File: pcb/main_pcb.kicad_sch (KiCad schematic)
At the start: 39 parts, among them J1 Conn_01x06_Socket, J2 Conn_01x10_Pin, J3 Conn_01x06_Pin, J4 USB_C_Receptacle_USB2.0, Q1 Si2323DS, SW1 SW_Push, SW2 SW_Push, SW3 SW_Push, U1 ESP32-H2-MINI-1, U2 LM5165Y

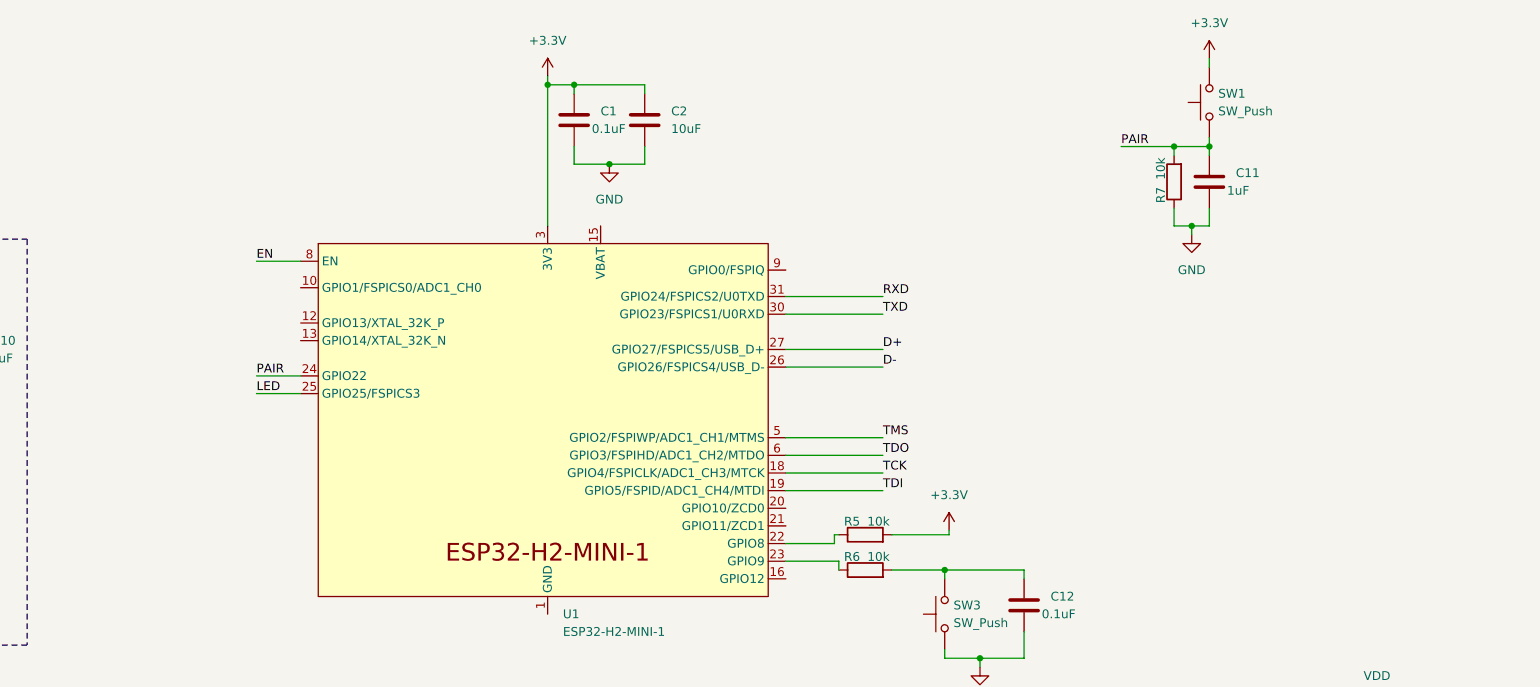
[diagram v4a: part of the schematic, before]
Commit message: Add RTC crystal circuit
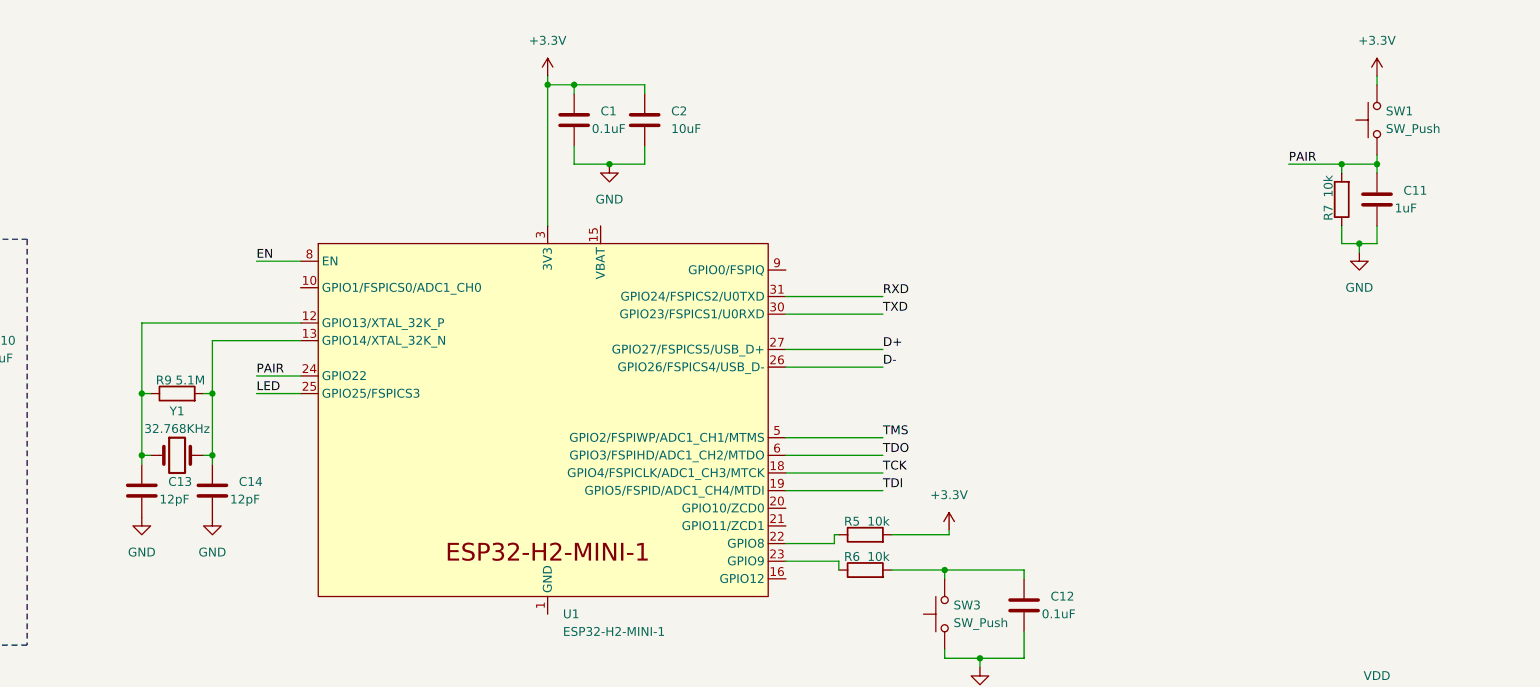
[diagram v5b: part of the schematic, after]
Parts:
- added C13, C14: 12pF, Capacitor_SMD:C_1206_3216Metric_Pad1.33x1.80mm_HandSolder, symbol Device:C
- added R9: 5.1M, Resistor_SMD:R_1206_3216Metric_Pad1.30x1.75mm_HandSolder, symbol Device:R
- added Y1: 32.768KHz, Crystal:Crystal_SMD_Abracon_ABS25-4Pin_8.0x3.8mm, symbol Device:Crystal
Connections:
- net GND: now also C13.2, C14.2
- net at U1.12 (GPIO13/XTAL_32K_P): now also C13.1, R9.1, Y1.1
- net at U1.13 (GPIO14/XTAL_32K_N): now also C14.1, R9.2, Y1.2
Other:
- moved on the sheet: C11, R7, SW1

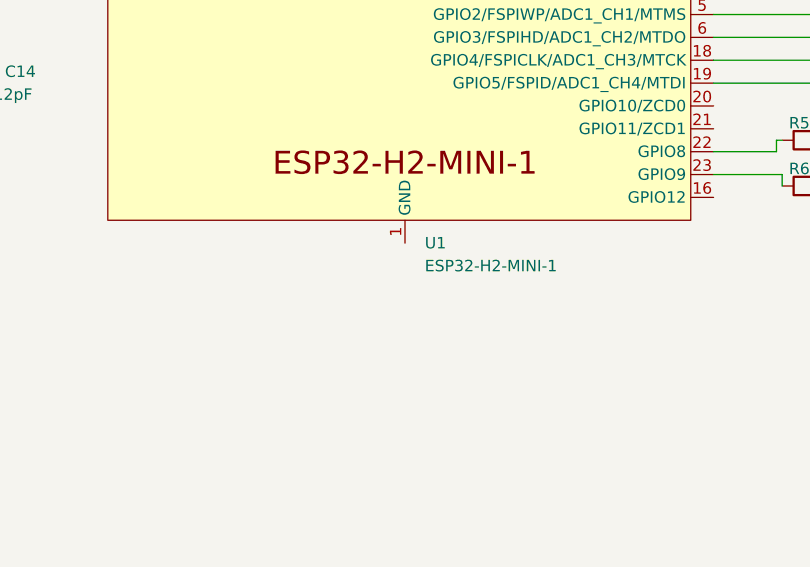
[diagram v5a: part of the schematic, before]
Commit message: Add GND connection to ESP32-H2
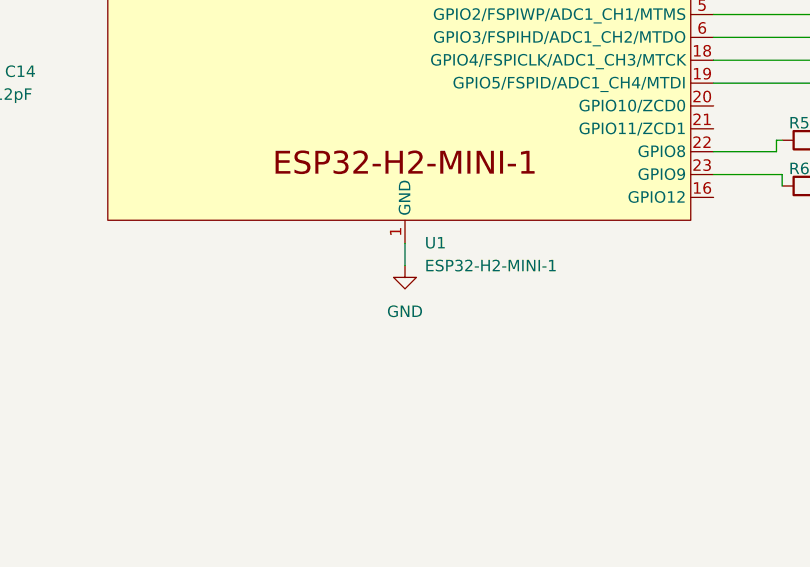
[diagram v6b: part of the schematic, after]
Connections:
- net GND: now also U1.1 (GND), U1.11 (GND), U1.14 (GND), U1.2 (GND), U1.36 (GND), U1.37 (GND), U1.38 (GND), U1.39 (GND), U1.40 (GND), U1.41 (GND), U1.42 (GND), U1.43 (GND), U1.44 (GND), U1.45 (GND), U1.46 (GND), U1.47 (GND), U1.48 (GND), U1.49 (GND), U1.50 (GND), U1.51 (GND), U1.52 (GND), U1.53 (GND)
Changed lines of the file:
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@@
+    (stroke (width 0) (type default))
+  )
+  (wire (pts (xy 158.75 105.41) (xy 158.75 107.95))
     (stroke (width 0) (type default))
   )
@@
         )
       )
+    )
+  )
+  (symbol (lib_id "power:GND") (at 158.75 107.95 0) (unit 1)
+    (in_bom yes) (on_board yes) (dnp no) (fields_autoplaced)
+    (property "Reference" "#PWR037" (at 158.75 114.3 0)
+      (effects (font (size 1.27 1.27)) hide)
+    )
+    (property "Value" "GND" (at 158.75 113.03 0)
+      (effects (font (size 1.27 1.27)))
+    )
+    (property "Footprint" "" (at 158.75 107.95 0)
+      (effects (font (size 1.27 1.27)) hide)
+    )
+    (property "Datasheet" "" (at 158.75 107.95 0)
+      (effects (font (size 1.27 1.27)) hide)
+    )
+    (pin "1")
+    (instances
+      (project "main_pcb"
+        (path "/6204b7c2-8814-41ee-9243-5078f55f08d4"
+          (reference "#PWR037") (unit 1)
+        )
+      )

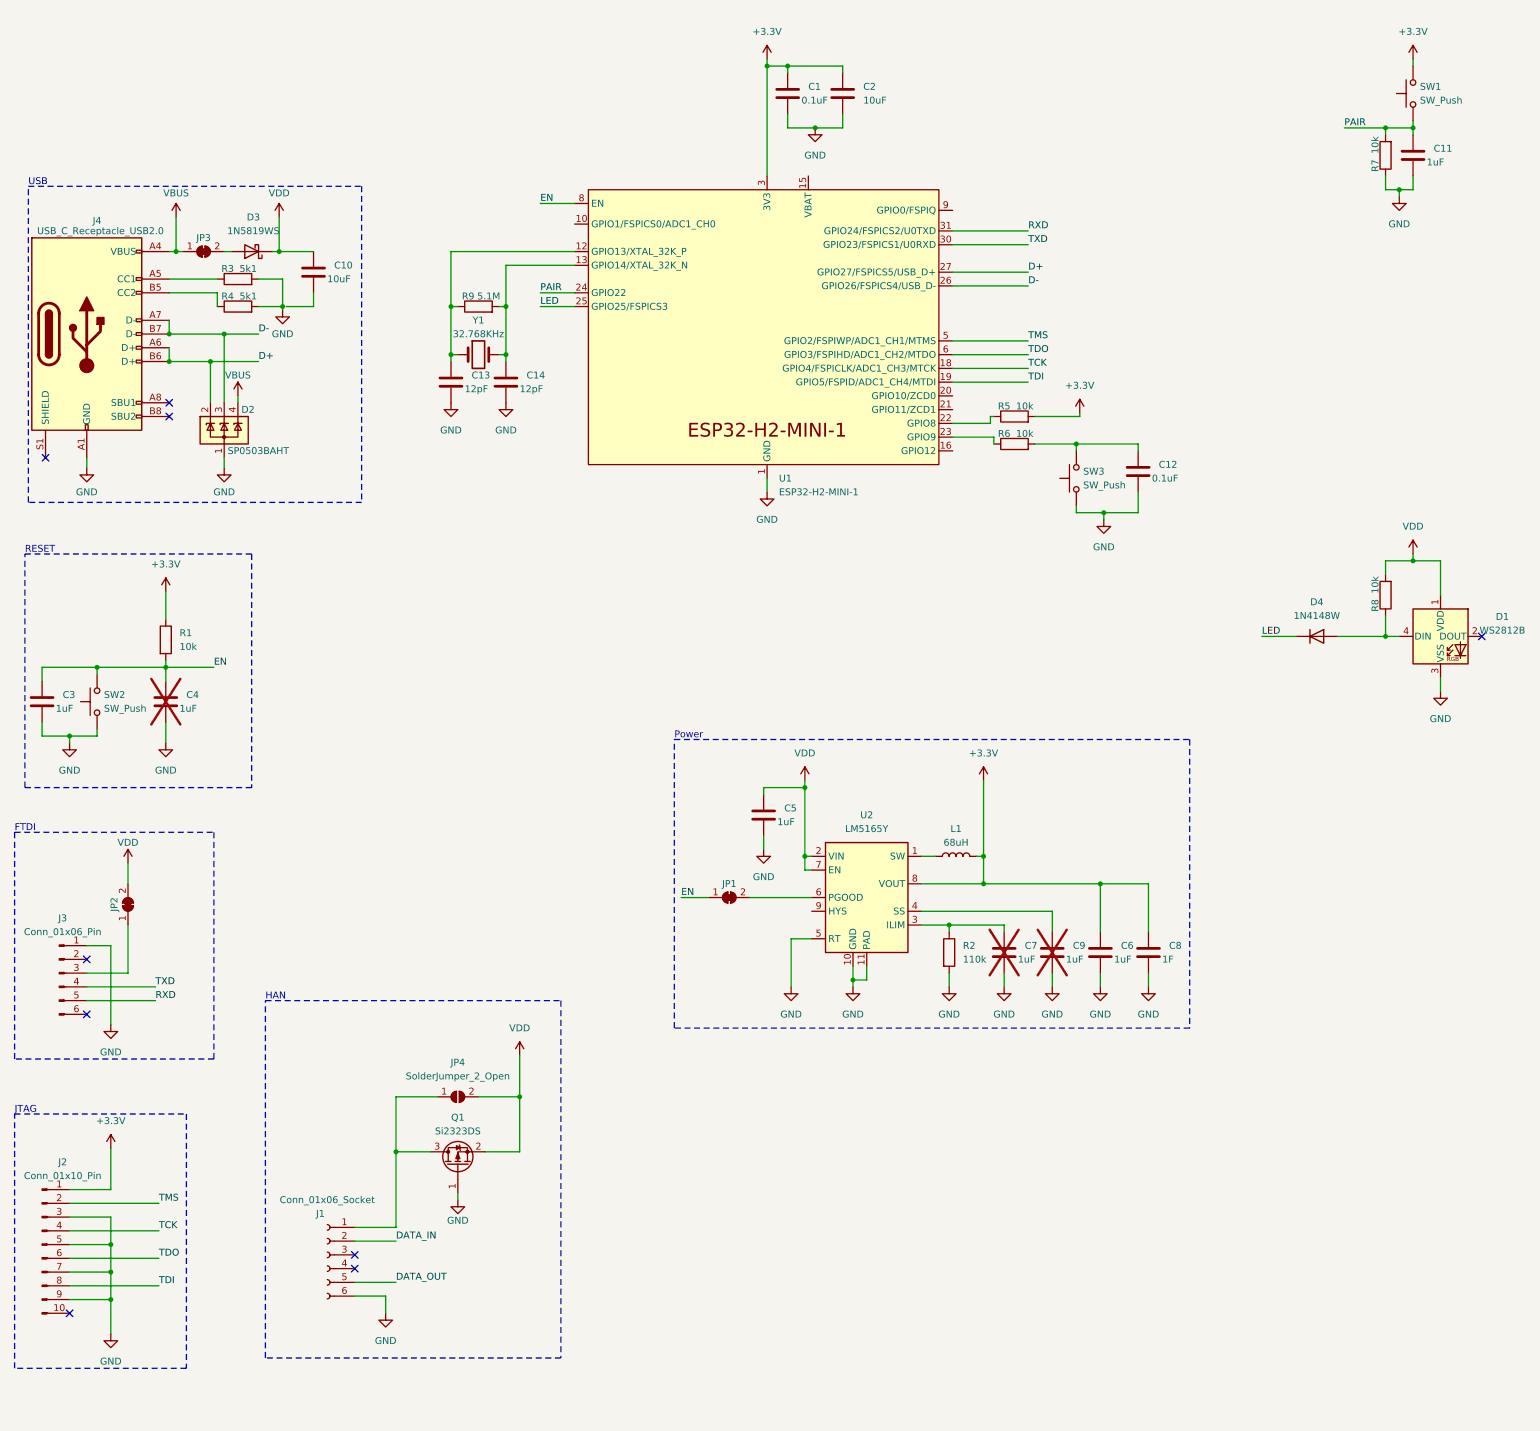
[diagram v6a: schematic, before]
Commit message: Remove FTDI connector
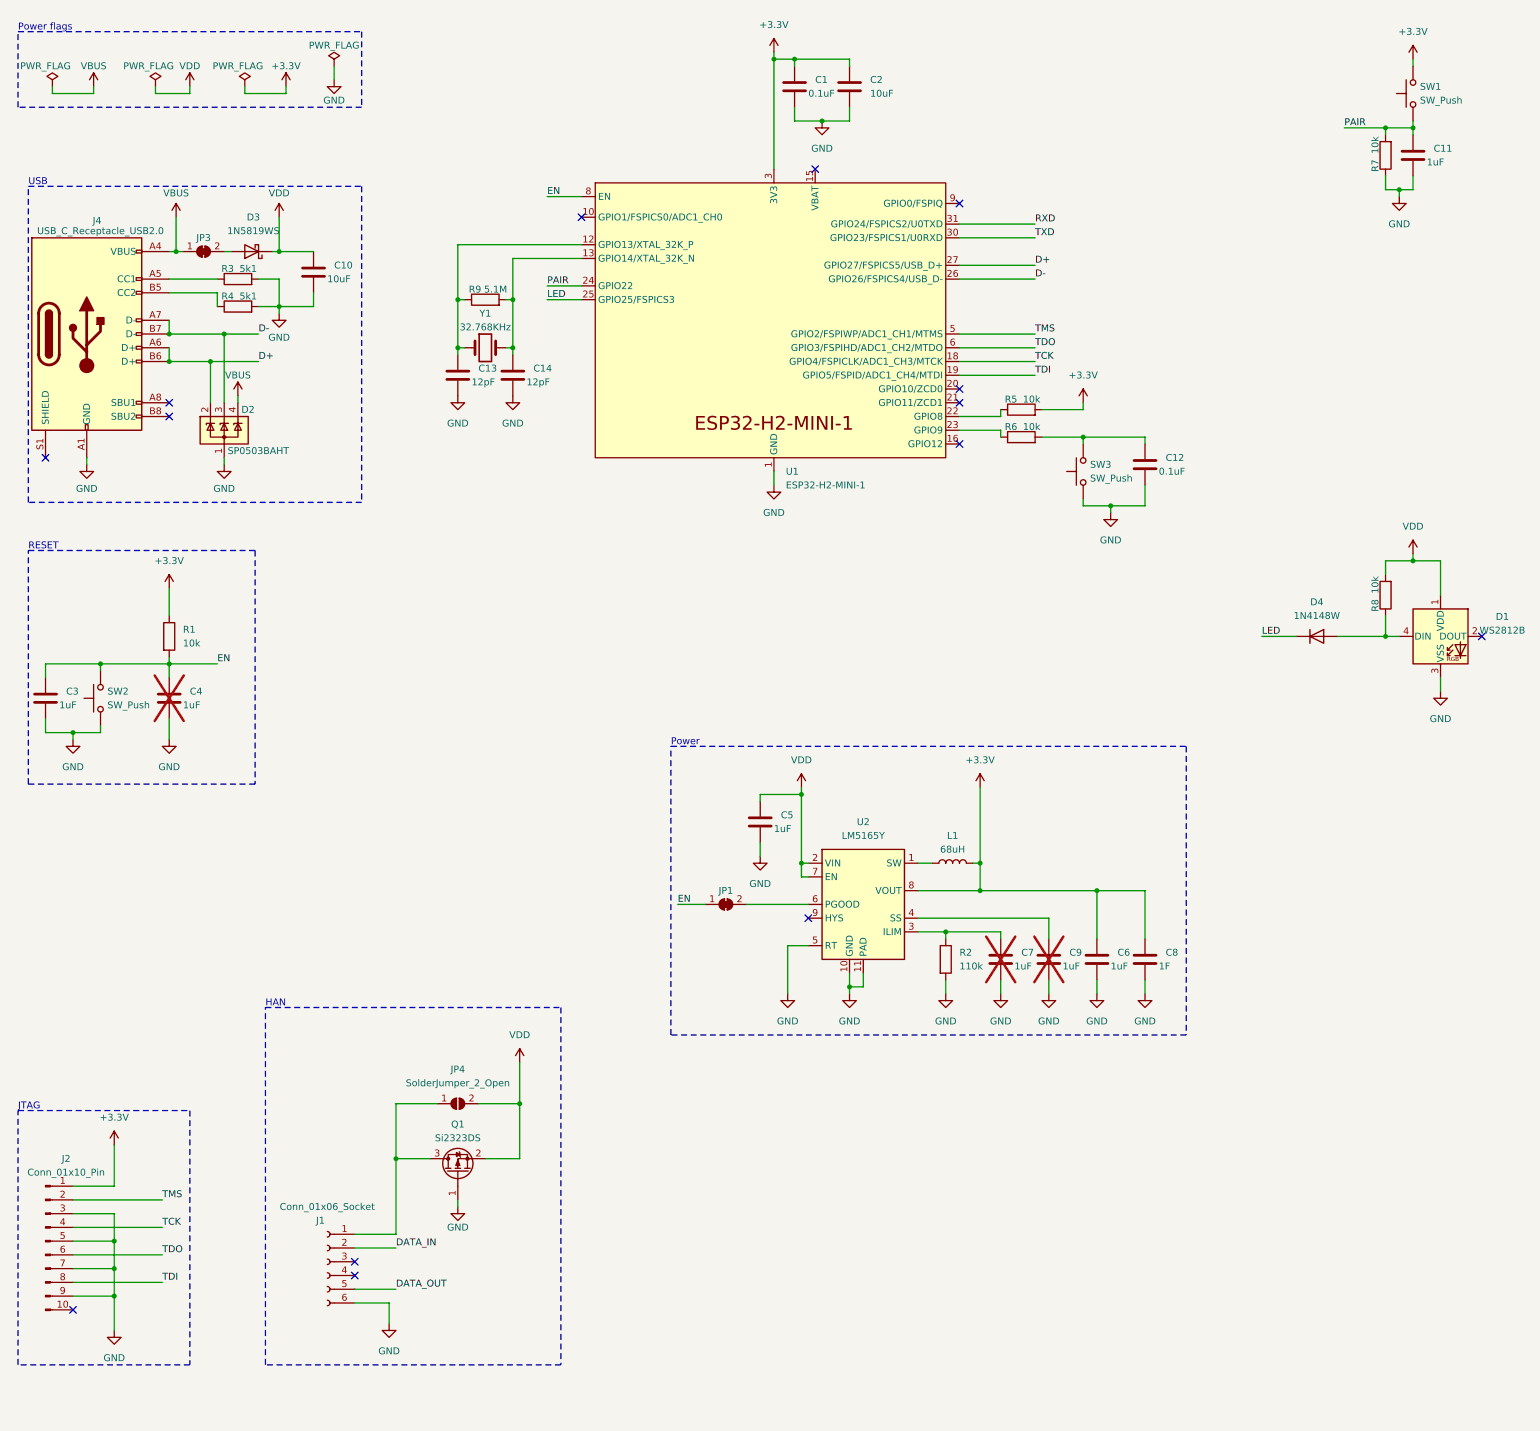
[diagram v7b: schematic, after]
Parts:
- removed J3: Conn_01x06_Pin, Connector_PinHeader_2.54mm:PinHeader_1x06_P2.54mm_Horizontal, symbol Connector:Conn_01x06_Pin
- removed JP2: SolderJumper_2_Bridged, Jumper:SolderJumper-2_P1.3mm_Open_TrianglePad1.0x1.5mm, symbol Jumper:SolderJumper_2_Bridged
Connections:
- net GND: now also C10.2
- no-connect marks 9 -> 14
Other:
- note added: "Power flags"
- note removed: "FTDI"
- moved on the sheet: C1, C12, C13, C14, C2, C3, C4, C5, C6, C7, C8, C9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

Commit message: Add HAN interface connections to ESP32
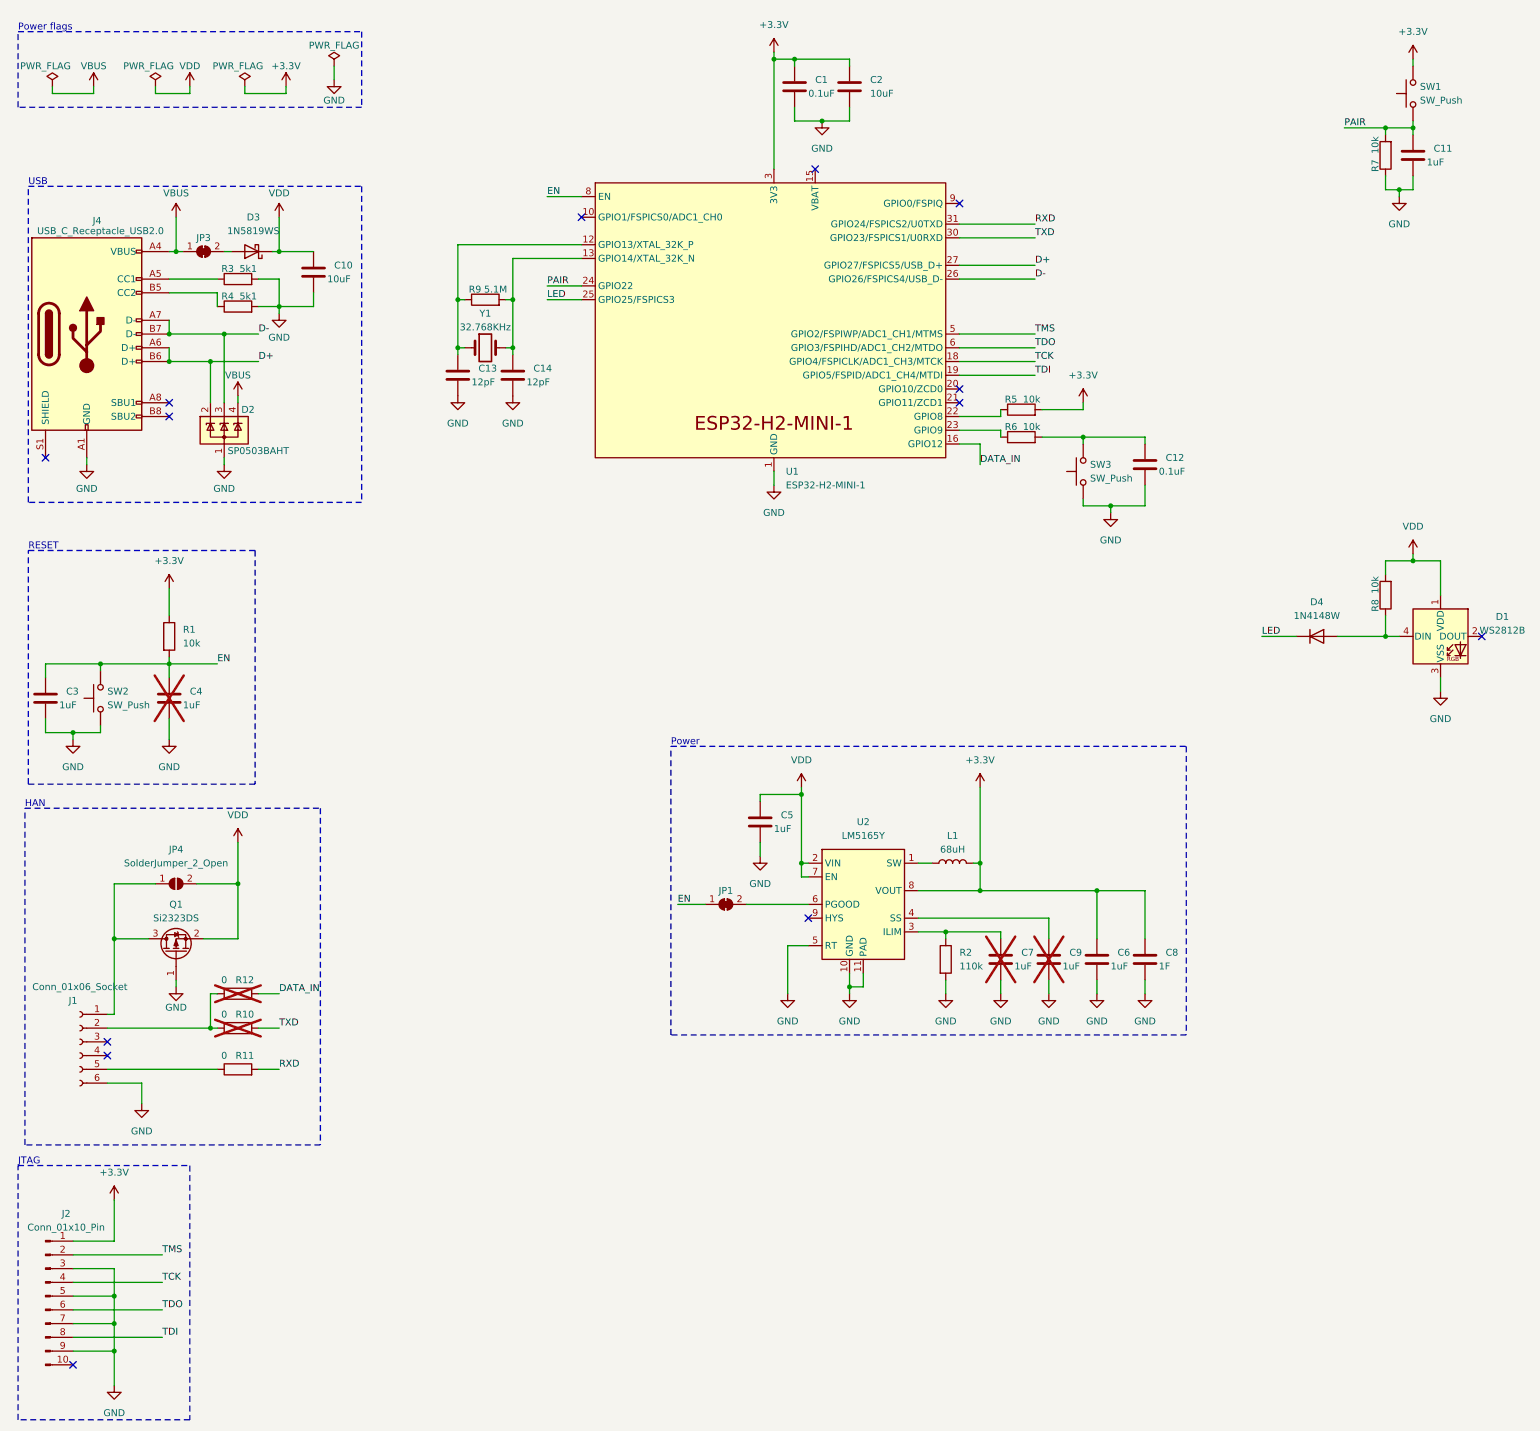
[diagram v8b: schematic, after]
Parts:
- added R10, R11, R12: 0, Resistor_SMD:R_1206_3216Metric_Pad1.30x1.75mm_HandSolder, symbol Device:R
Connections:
- net DATA_IN: now also U1.16 (GPIO12), R12.2; no longer J1.2 (Pin_2)
- net RXD: now also R11.2
- net TXD: now also R10.2
- net DATA_OUT: no longer names the net of J1.5 (Pin_5)
- net DATA_OUT: now also R11.1
- new net: J1.2 (Pin_2), R10.1, R12.1
- no-connect marks 14 -> 13
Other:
- moved on the sheet: J1, J2, JP4, Q1
